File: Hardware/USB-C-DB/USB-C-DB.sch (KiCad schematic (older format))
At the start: 64 parts, among them J1 USB_C_Receptacle, J2 BatTP+, J3 Battery con, J4 BatTP-, U1 FT260S-U

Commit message: Updating with alternative parts
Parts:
- removed C?: 0.1u, Capacitor_SMD:C_0805_2012Metric_Pad1.18x1.45mm_HandSolder, symbol Device:C
- removed R?: 1, Resistor_SMD:R_0603_1608Metric_Pad0.98x0.95mm_HandSolder, symbol Device:R_Shunt
- added C4: 10u, Capacitor_SMD:C_0805_2012Metric_Pad1.18x1.45mm_HandSolder, symbol Device:C
- added R7: 1, Resistor_SMD:R_0603_1608Metric_Pad0.98x0.95mm_HandSolder, symbol Device:R
- C1, C3: renamed from C?; MPN1 (none) -> C0402C470J5GACTU
- C11, C14, C15, C6, C9: renamed from C?; MPN1 (none) -> C0805C104M5RAC7800; MPN2 (none) -> C0805C104M5RACTU
- FB1: renamed from FB?; MPN1 (none) -> FBMH1608HM471-T
- J1: MPN1 (none) -> USB4105-GF-A
- J10, J11, J12, J13, J14, J15, J16, J17, J18, J19, J20, J21, J22, J7, J8, J9: renamed from J?; footprint TestPoint:TestPoint_Pad_D4.0mm -> TestPoint:TestPoint_Pad_D1.0mm
- J2, J3: renamed from J?; footprint TestPoint:TestPoint_THTPad_D4.0mm_Drill2.0mm -> TestPoint:TestPoint_THTPad_D1.0mm_Drill0.5mm
- J4: renamed from J2; footprint TestPoint:TestPoint_THTPad_D4.0mm_Drill2.0mm -> TestPoint:TestPoint_THTPad_D1.0mm_Drill0.5mm
- J6: renamed from J4; footprint TestPoint:TestPoint_THTPad_D4.0mm_Drill2.0mm -> TestPoint:TestPoint_THTPad_D1.0mm_Drill0.5mm
- R13, R3, R4: renamed from R?; MPN1 (none) -> RC0805JR-075K1L; MPN2 (none) -> CRCW08055K10JNEB
- U1: renamed from U?; footprint SOT65P210X110-6N -> Mouser-imports:SOT65P210X110-6N
- U2: renamed from U?; MPN1 (none) -> NCP1117LPST33T3G
- U3: renamed from U1; Supplier 1 Digi-Key -> (none); Supplier 2 Mouser -> (none)
- gave numbers to parts that had none: 26
- renumbered J3 to J5
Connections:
- no-connect marks 18 -> 10

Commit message: Adding OSHW logo on PCB
* Updating BOM with available parts for test run
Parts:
- C1, C3: MPN prod (none) -> C0402C470J5GACTU
- C10, C16, C2, C5, C7: MPN prod (none) -> CL21A475KAQNNNF
- C11, C14, C15, C6, C9: MPN prod (none) -> C0805C104M5RACTU
- C12, C13, C4, C8: MPN prod (none) -> CL21A106KOQNNNE
- FB1: MPN prod (none) -> FBMH1608HM471-T
- J1: MPN prod (none) -> USB4105-GF-A
- Q1, Q2: MPN prod (none) -> XP262N7002TR-G
- R1: MPN prod (none) -> RC0805FR-0713KL
- R10, R9: MPN prod (none) -> CRCW040211R0FKEDC
- R11, R12, R14, R15, R16, R17, R18, R19, R2, R6, R8: MPN prod (none) -> CRG0603F10K/10
- R13, R3, R4: MPN prod (none) -> RC0805JR-075K1L
- R5: MPN prod (none) -> RC0805FR-074K7P
- R7: MPN prod (none) -> RT0603FRE071RL
- U1: MPN prod (none) -> NUF2221W1T2G
- U2: MPN prod (none) -> NCP1117LPST33T3G
- U3: MPN prod (none) -> FT260S-U
- U4: MPN prod (none) -> ESP-WROOM-02D-N2

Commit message: Adding full layout for design
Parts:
- removed J5: Battery con, Connector_JST:JST_PH_B2B-PH-K_1x02_P2.00mm_Vertical, symbol Connector_Generic:Conn_01x02
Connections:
- net labels added: UART_TRX_N, UART_TRX_P
- net labels removed: UART_RX_N, UART_TX_P
- wire segments 244 -> 240
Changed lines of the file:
@@
 	1    0    0    -1
 $EndComp
-$Comp
-L Connector_Generic:Conn_01x02 J5
-U 1 1 61326DA4
-P 2310 1310
-F 0 "J5" H 2390 1302 50  0000 L CNN
-F 1 "Battery con" H 2390 1211 50  0000 L CNN
-F 2 "Connector_JST:JST_PH_B2B-PH-K_1x02_P2.00mm_Vertical" H 2310 1310 50  0001 C CNN
-F 3 "~" H 2310 1310 50  0001 C CNN
-F 4 "" H 2310 1310 50  0001 C CNN "MPN"
-	1    2310 1310
-	1    0    0    -1
-$EndComp
 Wire Wire Line
 	2110 1170 2020 1170
@@
 	2020 1170 2020 1240
 Wire Wire Line
-	2020 1310 2110 1310
-Wire Wire Line
 	2020 1530 2110 1530
-Wire Wire Line
-	2020 1410 2110 1410
 $Comp
 L power:-BATT #PWR05
@@
 $EndComp
 Wire Wire Line
-	2020 1410 2020 1470
-Wire Wire Line
 	1960 1240 2020 1240
-Connection ~ 2020 1240
-Wire Wire Line
-	2020 1240 2020 1310
 Wire Wire Line
 	1960 1470 2020 1470
-Connection ~ 2020 1470
 Wire Wire Line
 	2020 1470 2020 1530
@@
 VBUS_ISEN-
 Text Label 6350 3750 2    50   ~ 0
-UART_RX_N
+UART_TRX_N
 Text Label 6350 3650 2    50   ~ 0
-UART_TX_P
+UART_TRX_P
 Wire Wire Line
 	6350 3750 5950 3750
@@
 	7250 5350 7700 5350
 Text Label 7250 5350 0    50   ~ 0
-UART_TX_P
+UART_TRX_P
 Text Label 7250 5450 0    50   ~ 0
-UART_RX_N
+UART_TRX_N
 Wire Wire Line
 	8200 4650 8200 4600

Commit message: Updating schematic to replace FT260 for FT231
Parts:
- removed C10, C2, C7: 4.7u, Capacitor_SMD:C_0805_2012Metric_Pad1.18x1.45mm_HandSolder, symbol Device:C
- removed C9: 0.1u, Capacitor_SMD:C_0805_2012Metric_Pad1.18x1.45mm_HandSolder, symbol Device:C
- removed J1: USB_C_Receptacle, Connector_USB:USB_C_Receptacle_HRO_TYPE-C-31-M-12, symbol USB-C-DB-rescue:USB_C_Receptacle-Connector
- removed J13: MCU_TOUT, TestPoint:TestPoint_Pad_D1.0mm, symbol Connector_Generic:Conn_01x01
- removed J15: EFUSE_PRG, TestPoint:TestPoint_Pad_D1.0mm, symbol Connector_Generic:Conn_01x01
- removed J18: NOT_SUSP, TestPoint:TestPoint_Pad_D1.0mm, symbol Connector_Generic:Conn_01x01
- removed J2: EFPROG_POS, TestPoint:TestPoint_THTPad_D1.0mm_Drill0.5mm, symbol Connector_Generic:Conn_01x01
- removed J22: DEBUGGER, TestPoint:TestPoint_Pad_D1.0mm, symbol Connector_Generic:Conn_01x01
- removed J3: EFPROG_NEG, TestPoint:TestPoint_THTPad_D1.0mm_Drill0.5mm, symbol Connector_Generic:Conn_01x01
- removed J4: BatTP+, TestPoint:TestPoint_THTPad_D1.0mm_Drill0.5mm, symbol Connector_Generic:Conn_01x01
- removed J6: BatTP-, TestPoint:TestPoint_THTPad_D1.0mm_Drill0.5mm, symbol Connector_Generic:Conn_01x01
- removed R10, R9: 11, Resistor_SMD:R_0402_1005Metric_Pad0.72x0.64mm_HandSolder, symbol Device:R
- removed R11, R12, R14, R6, R8: 10k, Resistor_SMD:R_0603_1608Metric_Pad0.98x0.95mm_HandSolder, symbol Device:R
- removed R13: 5.1k, Resistor_SMD:R_0805_2012Metric_Pad1.20x1.40mm_HandSolder, symbol Device:R
- removed U3: FT260S-U, Mouser-imports:SOP65P640X120-28N, symbol USB-C-DB-rescue:FT260S-U
- added C5: 0.1u, Capacitor_SMD:C_0805_2012Metric_Pad1.18x1.45mm_HandSolder, symbol Device:C
- added D1, D2, D3: LED, LED_SMD:LED_Cree-PLCC4_3.2x2.8mm_CCW, symbol Device:LED
- added J1: USB4105-GF-A, SnapEDA-imports:GCT_USB4105-GF-A, symbol USB-C-DB-rescue:USB4105-GF-A
- added R5: 309, Resistor_SMD:R_0603_1608Metric_Pad0.98x0.95mm_HandSolder, symbol Device:R
- added U3: FT231XS, Package_SO:SSOP-20_3.9x8.7mm_P0.635mm, symbol USB-C-DB-rescue:FT231XS
- R1: value 13k -> 309; footprint Resistor_SMD:R_0805_2012Metric_Pad1.20x1.40mm_HandSolder -> Resistor_SMD:R_0603_1608Metric_Pad0.98x0.95mm_HandSolder; MPN RC0805FR-0713KL -> RC0603FR-07309RL; MPN prod RC0805FR-0713KL -> RC0603FR-07309RL
- R2: value 10k -> 309; MPN CRG0603F10K/10 -> RC0603FR-07309RL; MPN prod CRG0603F10K/10 -> RC0603FR-07309RL
- renumbered C4 to C1, C13 to C10, C14 to C11, C15 to C12, C16 to C13, C1 to C2, C8 to C4, C5 to C6, C6 to C7, C11 to C8, C12 to C9, J16 to J10, J17 to J11, J19 to J12, J20 to J13, J21 to J14, J7 to J2, J8 to J3, J9 to J4, J10 to J5, J11 to J6, J12 to J7, J14 to J9, R17 to R10, R18 to R11, R19 to R12, R7 to R6, R5 to R7, R15 to R8, R16 to R9, U2 to U1, U1 to U2
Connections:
- net labels added: POWER_SHDN, RXLED, TXLED, USBC_N, USBC_P
- net labels removed: +BATT, -BATT, DEBUGGER, EFUSE_PROG, NOT_SUSP, STEST_RSTN, VOUT3V3
- wire segments 240 -> 200
- no-connect marks 10 -> 6
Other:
- note added: "28-08-2022"
- note added: "Put in USB Bus Powered mode"
- note added: "Test points"
- note added: "Transmit LEDs\n (White)"
- note added: "USB suspend mode\nindicatior LED\n (White)"
- note added: "v2.0.0"
- note removed: "09-03-2022"
- note removed: "Battery connector"
- note removed: "Exchange TXD and RXD with RTS\n and CTS in MCU if UART0's default\n info message is caussing issues."
- note removed: "Pull DCNF1 HIGH and DCNF0 LOW\n to enable only UART\n (DIO3 as RXD, DIO4 as TXD)"
- note removed: "Test points (top side)"
- note removed: "USB controller set to use a\n Bus Powered Configuration"
- note removed: "v0.6.1"
- moved on the sheet: C1, C4, C6, C7, C8, J10, J11, J12, J13, J14, J2, J3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

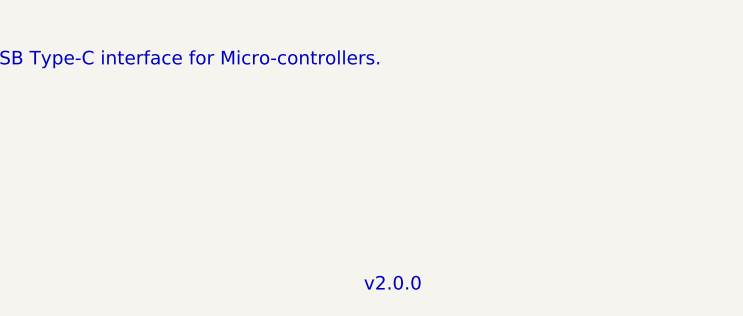
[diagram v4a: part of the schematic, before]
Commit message: Updating layout to replace FT260 for FT231
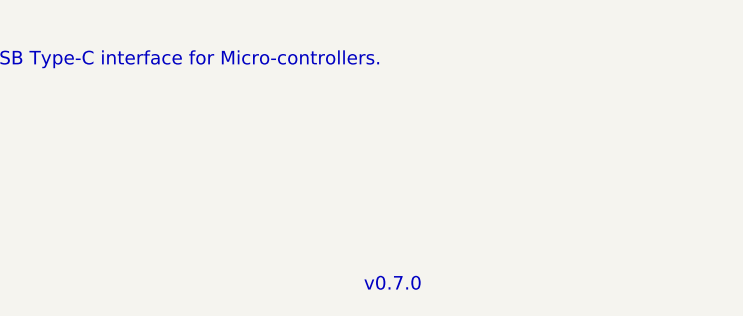
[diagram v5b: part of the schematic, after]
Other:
- note added: "v0.7.0"
- note removed: "v2.0.0"
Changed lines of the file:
@@
 USB-C demo board for Micro-controllers
 Text Notes 10570 7635 0    59   ~ 0
-v2.0.0
+v0.7.0
 Text Notes 8105 7635 0    50   ~ 0
 28-08-2022
@@
 Wire Wire Line
 	4350 3650 4050 3650
+Text Label 4050 3650 0    50   ~ 0
+USBC_N
+Text Label 4050 3750 0    50   ~ 0
+USBC_P
 Wire Bus Line
 	7000 1100 7000 1700
@@
 Wire Bus Line
 	9400 4900 9400 5450
-Text Label 4050 3650 0    50   ~ 0
-USBC_N
-Text Label 4050 3750 0    50   ~ 0
-USBC_P
 $EndSCHEMATC

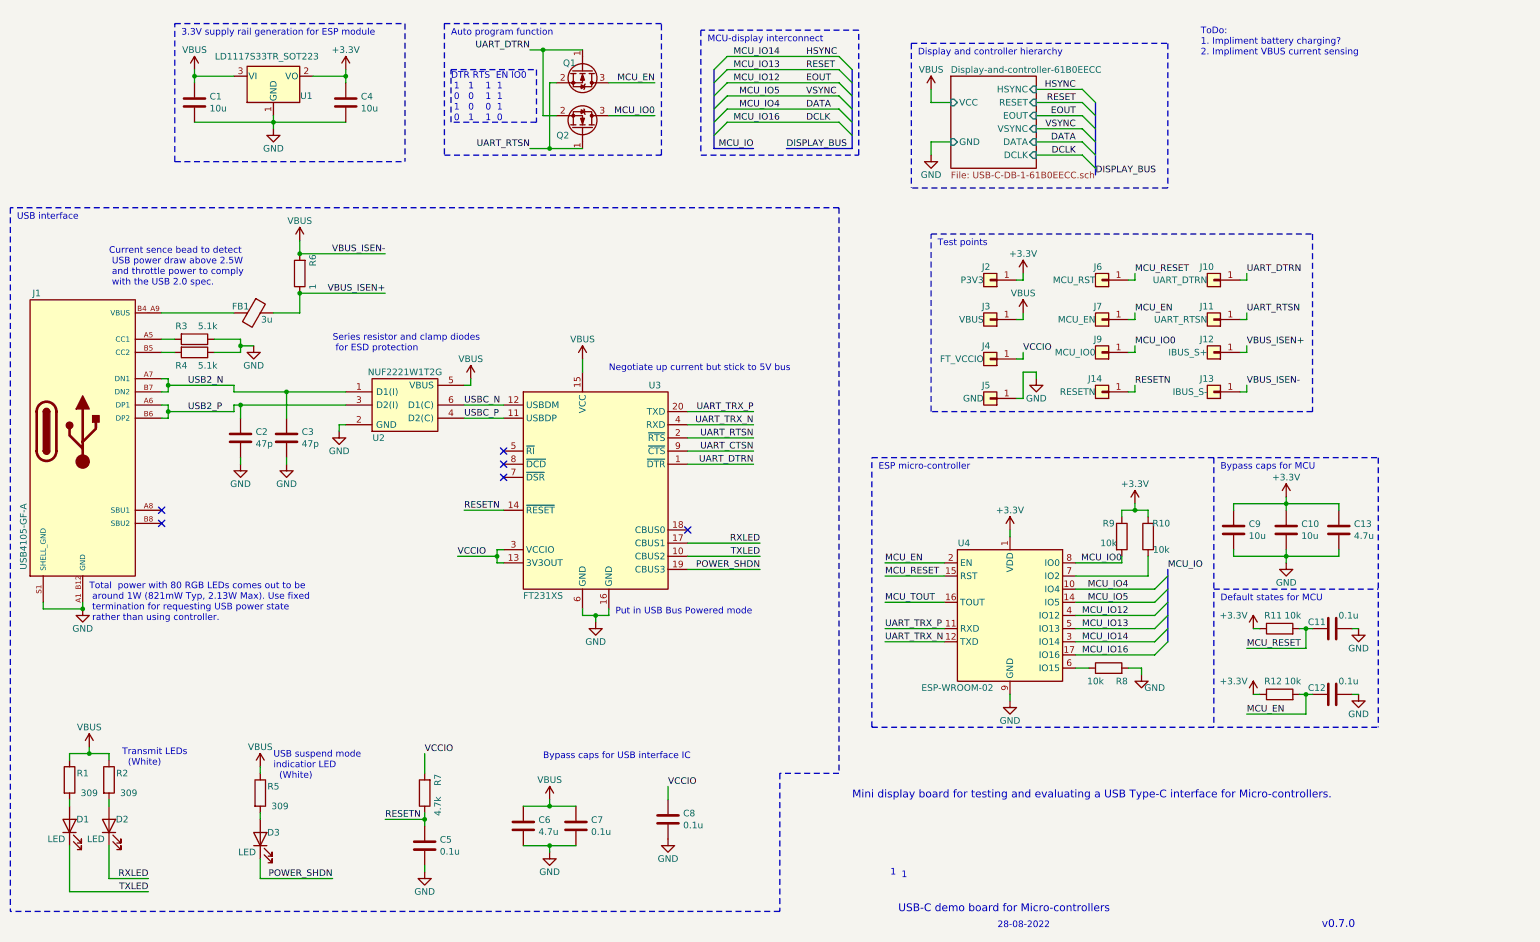
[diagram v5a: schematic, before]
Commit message: Fixing incorrect connection in debug LEDs
* Updating symbol to fix incorrect GND connection in debug LED
* Adding image of assembled demo
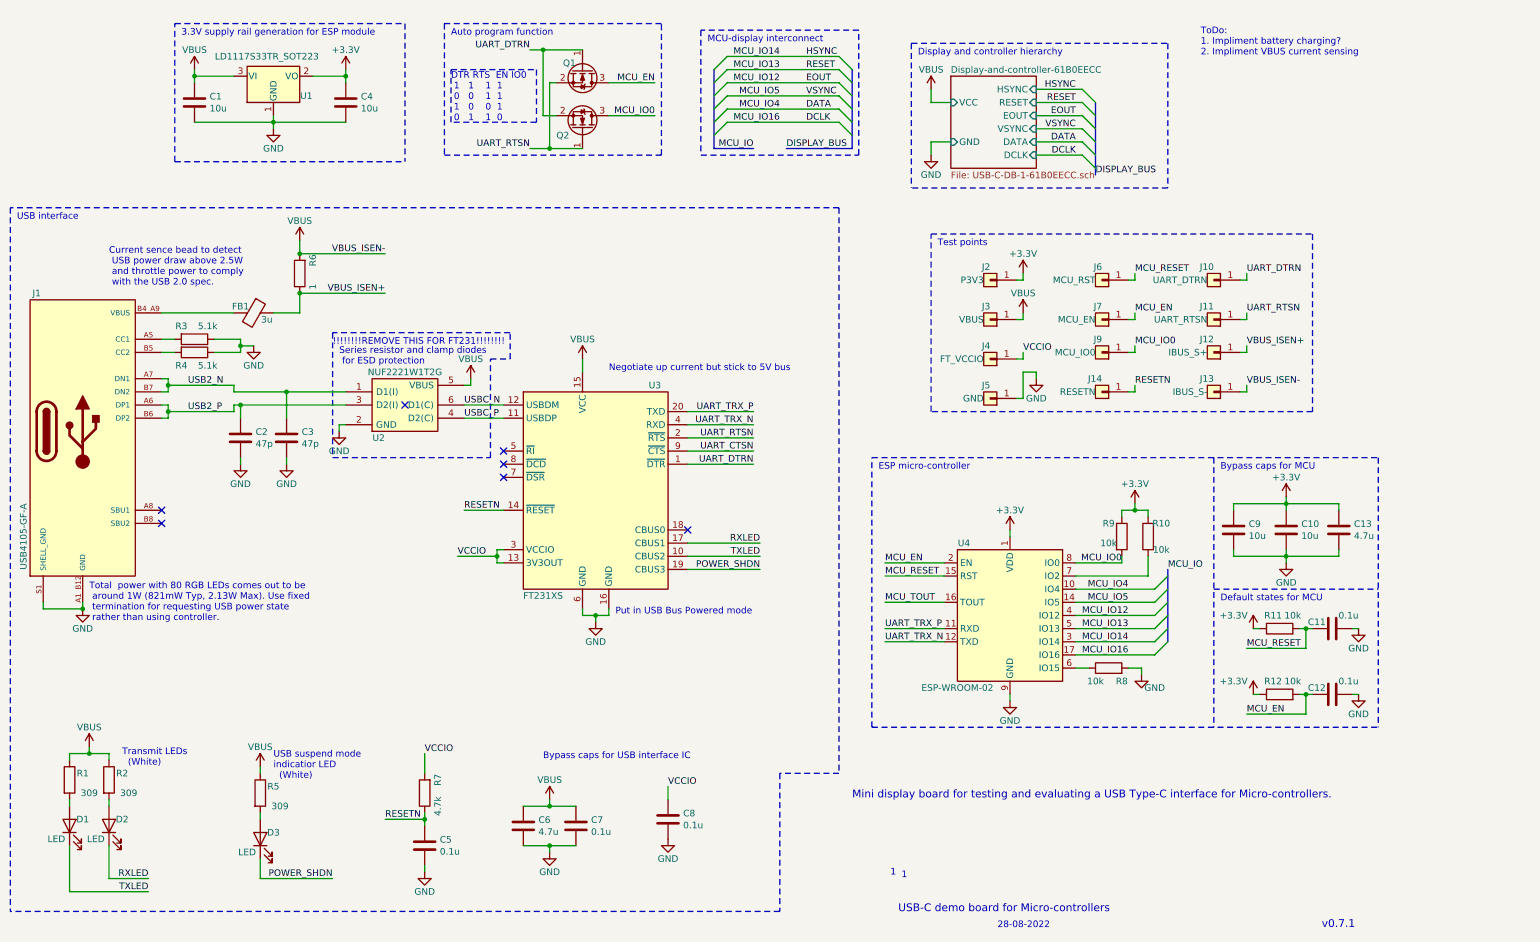
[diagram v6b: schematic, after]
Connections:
- no-connect marks 6 -> 7
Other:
- note added: "!!!!!!!!REMOVE THIS FOR FT231!!!!!!!!"
- note added: "v0.7.1"
- note removed: "v0.7.0"
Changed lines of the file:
@@
 USB-C demo board for Micro-controllers
 Text Notes 10570 7635 0    59   ~ 0
-v0.7.0
+v0.7.1
 Text Notes 8105 7635 0    50   ~ 0
 28-08-2022
@@
 Wire Wire Line
 	1800 3500 2300 3500
-Text Notes 3050 3250 0    50   ~ 0
+Text Notes 3100 3350 0    50   ~ 0
 Series resistor and clamp diodes\n for ESD protection
 $Comp
@@
 Text Label 4050 3750 0    50   ~ 0
 USBC_P
+NoConn ~ 3600 3650
+Text Notes 3050 3200 0    50   ~ 0
+!!!!!!!!REMOVE THIS FOR FT231!!!!!!!!
+Wire Notes Line
+	3050 3100 3050 4050
+Wire Notes Line
+	3050 4050 4250 4050
+Wire Notes Line
+	4250 4050 4250 3300
+Wire Notes Line
+	4250 3300 4400 3300
+Wire Notes Line
+	4400 3300 4400 3100
+Wire Notes Line
+	4400 3100 3050 3100
 Wire Bus Line
 	7000 1100 7000 1700

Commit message: Patching activity LED connections and adding FTDI firmware
* Patching issue in layout where the FTDI activity LED orientations where incorrectly connected.
* Adding firmware template and instructions to modify the FT231's EEPROM firmware
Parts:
- D1, D2, D3: symbol Device:LED -> USB-C-DB-rescue:LED
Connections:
- net GND: no longer U2.2 (GND)
- net POWER_SHDN: now also D3.4 (K); no longer D3.1 (K)
- net RXLED: now also D2.4 (K); no longer D2.1 (K)
- net TXLED: now also D1.4 (K); no longer D1.1 (K)
- net VBUS: no longer U2.5 (VBUS)
- no-connect marks 7 -> 8
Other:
- note added: "(disconnected clamps,\nas they are not compatable\nwith FT231)"
- note added: "17-03-2023"
- note added: "Series resistors"
- note added: "v0.7.2"
- note removed: "!!!!!!!!REMOVE THIS FOR FT231!!!!!!!!"
- note removed: "28-08-2022"
- note removed: "Series resistor and clamp diodes\n for ESD protection"
- note removed: "v0.7.1"
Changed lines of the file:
@@
 USB-C demo board for Micro-controllers
 Text Notes 10570 7635 0    59   ~ 0
-v0.7.1
+v0.7.2
 Text Notes 8105 7635 0    50   ~ 0
-28-08-2022
+17-03-2023
 Text Notes 7290 7235 0    50   ~ 0
 1
@@
 Wire Wire Line
 	1800 3500 2300 3500
-Text Notes 3100 3350 0    50   ~ 0
-Series resistor and clamp diodes\n for ESD protection
+Text Notes 3300 3300 0    50   ~ 0
+Series resistors
 $Comp
 L Device:C C2
@@
 Wire Wire Line
 	3750 6800 3750 6850
-$Comp
-L USB-C-DB-rescue:NUF2221W1T2G U2
-U 1 1 621665F6
-P 3600 3650
-F 0 "U2" H 3400 3400 50  0000 C CNN
-F 1 "NUF2221W1T2G" H 3600 3900 50  0000 C CNN
-F 2 "Mouser-imports:SOT65P210X110-6N" H 4650 3750 50  0001 L CNN
-F 3 "http://www.onsemi.com/pub/Collateral/NUF2221W1T2-D.PDF" H 4650 3650 50  0001 L CNN
-F 4 "USB Upstream Terminator with ESD Protection" H 4650 3550 50  0001 L CNN "Description"
-F 5 "1.1" H 4650 3450 50  0001 L CNN "Height"
-F 6 "863-NUF2221W1T2G" H 4650 3350 50  0001 L CNN "Mouser Part Number"
-F 7 "https://www.mouser.co.uk/ProductDetail/ON-Semiconductor/NUF2221W1T2G/?qs=ZXBb0xZ9WeBhigCT%252BMBgKA%3D%3D" H 4650 3250 50  0001 L CNN "Mouser Price/Stock"
-F 8 "ON Semiconductor" H 4650 3150 50  0001 L CNN "Manufacturer_Name"
-F 9 "NUF2221W1T2G" H 4650 3050 50  0001 L CNN "Manufacturer_Part_Number"
-F 10 "NUF2221W1T2G" H 3600 3650 50  0001 C CNN "MPN"
-F 11 "NUF2221W1T2G" H 3600 3650 50  0001 C CNN "MPN prod"
-	1    3600 3650
-	1    0    0    -1
-$EndComp
-$Comp
-L power:GND #PWR011
-U 1 1 621E9CAA
-P 3100 3850
-F 0 "#PWR011" H 3100 3600 50  0001 C CNN
-F 1 "GND" H 3100 3700 50  0000 C CNN
-F 2 "" H 3100 3850 50  0001 C CNN
-F 3 "" H 3100 3850 50  0001 C CNN
-	1    3100 3850
-	1    0    0    -1
-$EndComp
-Wire Wire Line
-	3100 3850 3100 3800
-Wire Wire Line
-	3100 3800 3150 3800
-$Comp
-L power:VBUS #PWR013
-U 1 1 621F1E3A
-P 4100 3450
-F 0 "#PWR013" H 4100 3300 50  0001 C CNN
-F 1 "VBUS" H 4100 3600 50  0000 C CNN
-F 2 "" H 4100 3450 50  0001 C CNN
-F 3 "" H 4100 3450 50  0001 C CNN
-	1    4100 3450
-	1    0    0    -1
-$EndComp
-Wire Wire Line
-	4100 3450 4100 3500
-Wire Wire Line
-	4100 3500 4050 3500
 Wire Notes Line
 	6450 7500 600  7500
@@
 	1050 6650 1050 6700
 $Comp
-L Device:LED D1
+L USB-C-DB-rescue:LED D1
 U 1 1 6344B96E
 P 1050 6850
@@
 $EndComp
 $Comp
-L Device:LED D2
+L USB-C-DB-rescue:LED D2
 U 1 1 6344B976
 P 1350 6850
@@
 	2500 6800 2500 6750
 $Comp
-L Device:LED D3
+L USB-C-DB-rescue:LED D3
 U 1 1 63564B93
 P 2500 6950
@@
 Text Label 4050 3750 0    50   ~ 0
 USBC_P
-NoConn ~ 3600 3650
-Text Notes 3050 3200 0    50   ~ 0
-!!!!!!!!REMOVE THIS FOR FT231!!!!!!!!
-Wire Notes Line
-	3050 3100 3050 4050
-Wire Notes Line
-	3050 4050 4250 4050
-Wire Notes Line
-	4250 4050 4250 3300
-Wire Notes Line
-	4250 3300 4400 3300
-Wire Notes Line
-	4400 3300 4400 3100
-Wire Notes Line
-	4400 3100 3050 3100
+NoConn ~ 4050 3500
+NoConn ~ 3150 3800
+$Comp
+L USB-C-DB-rescue:NUF2221W1T2G U2
+U 1 1 621665F6
+P 3600 3650
+F 0 "U2" H 3400 3400 50  0000 C CNN
+F 1 "NUF2221W1T2G" H 3600 3900 50  0000 C CNN
+F 2 "Mouser-imports:SOT65P210X110-6N" H 4650 3750 50  0001 L CNN
+F 3 "http://www.onsemi.com/pub/Collateral/NUF2221W1T2-D.PDF" H 4650 3650 50  0001 L CNN
+F 4 "USB Upstream Terminator with ESD Protection" H 4650 3550 50  0001 L CNN "Description"
+F 5 "1.1" H 4650 3450 50  0001 L CNN "Height"
+F 6 "863-NUF2221W1T2G" H 4650 3350 50  0001 L CNN "Mouser Part Number"
+F 7 "https://www.mouser.co.uk/ProductDetail/ON-Semiconductor/NUF2221W1T2G/?qs=ZXBb0xZ9WeBhigCT%252BMBgKA%3D%3D" H 4650 3250 50  0001 L CNN "Mouser Price/Stock"
+F 8 "ON Semiconductor" H 4650 3150 50  0001 L CNN "Manufacturer_Name"
+F 9 "NUF2221W1T2G" H 4650 3050 50  0001 L CNN "Manufacturer_Part_Number"
+F 10 "NUF2221W1T2G" H 3600 3650 50  0001 C CNN "MPN"
+F 11 "NUF2221W1T2G" H 3600 3650 50  0001 C CNN "MPN prod"
+	1    3600 3650
+	1    0    0    -1
+$EndComp
 Wire Bus Line
 	7000 1100 7000 1700
@@
 Wire Bus Line
 	9400 4900 9400 5450
+Text Notes 3100 4200 0    50   ~ 0
+(disconnected clamps,\nas they are not compatable\nwith FT231)
 $EndSCHEMATC

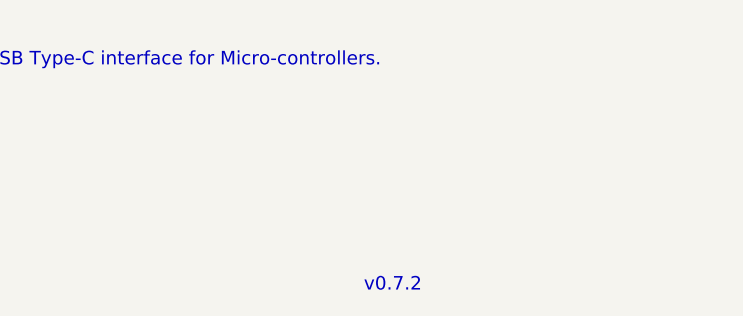
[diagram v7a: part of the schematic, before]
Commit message: Updating OSHW logo to include mechanicals
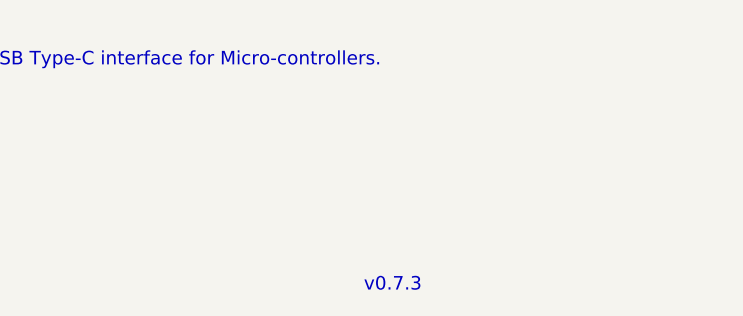
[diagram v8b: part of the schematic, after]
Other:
- note added: "v0.7.3"
- note removed: "v0.7.2"
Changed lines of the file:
@@
 USB-C demo board for Micro-controllers
 Text Notes 10570 7635 0    59   ~ 0
-v0.7.2
+v0.7.3
 Text Notes 8105 7635 0    50   ~ 0
 17-03-2023
@@
 	1    0    0    -1
 $EndComp
+Text Notes 3100 4200 0    50   ~ 0
+(disconnected clamps,\nas they are not compatable\nwith FT231)
 Wire Bus Line
 	7000 1100 7000 1700
@@
 Wire Bus Line
 	9400 4900 9400 5450
-Text Notes 3100 4200 0    50   ~ 0
-(disconnected clamps,\nas they are not compatable\nwith FT231)
 $EndSCHEMATC
